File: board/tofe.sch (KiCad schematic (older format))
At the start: 16 parts, among them P301 TOFE I2C, P302 TOFE-8X, P303 DEBUG, U301 24AA01/24LC01B

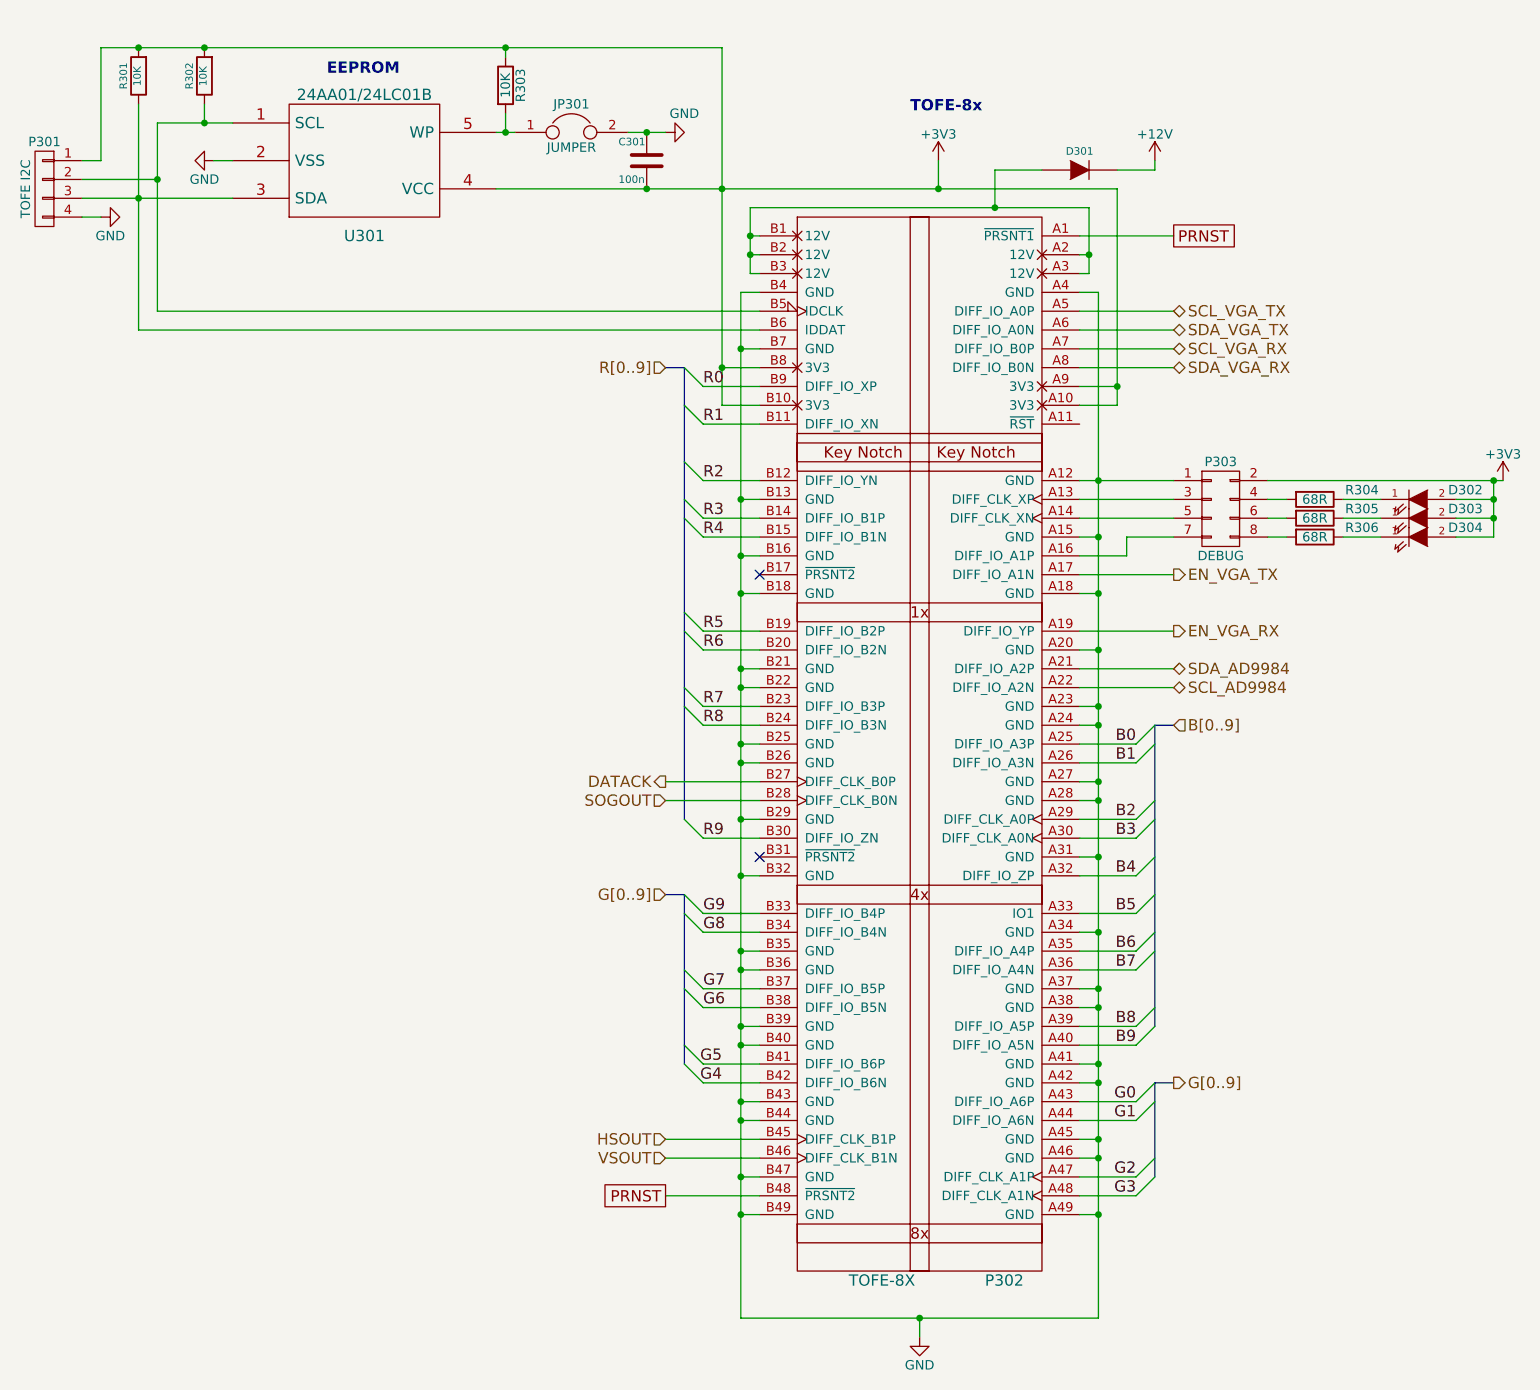
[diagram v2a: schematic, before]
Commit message: Lots of small tweaks.
 * Giving things better reference names.
 * Giving a bunch of nets names.
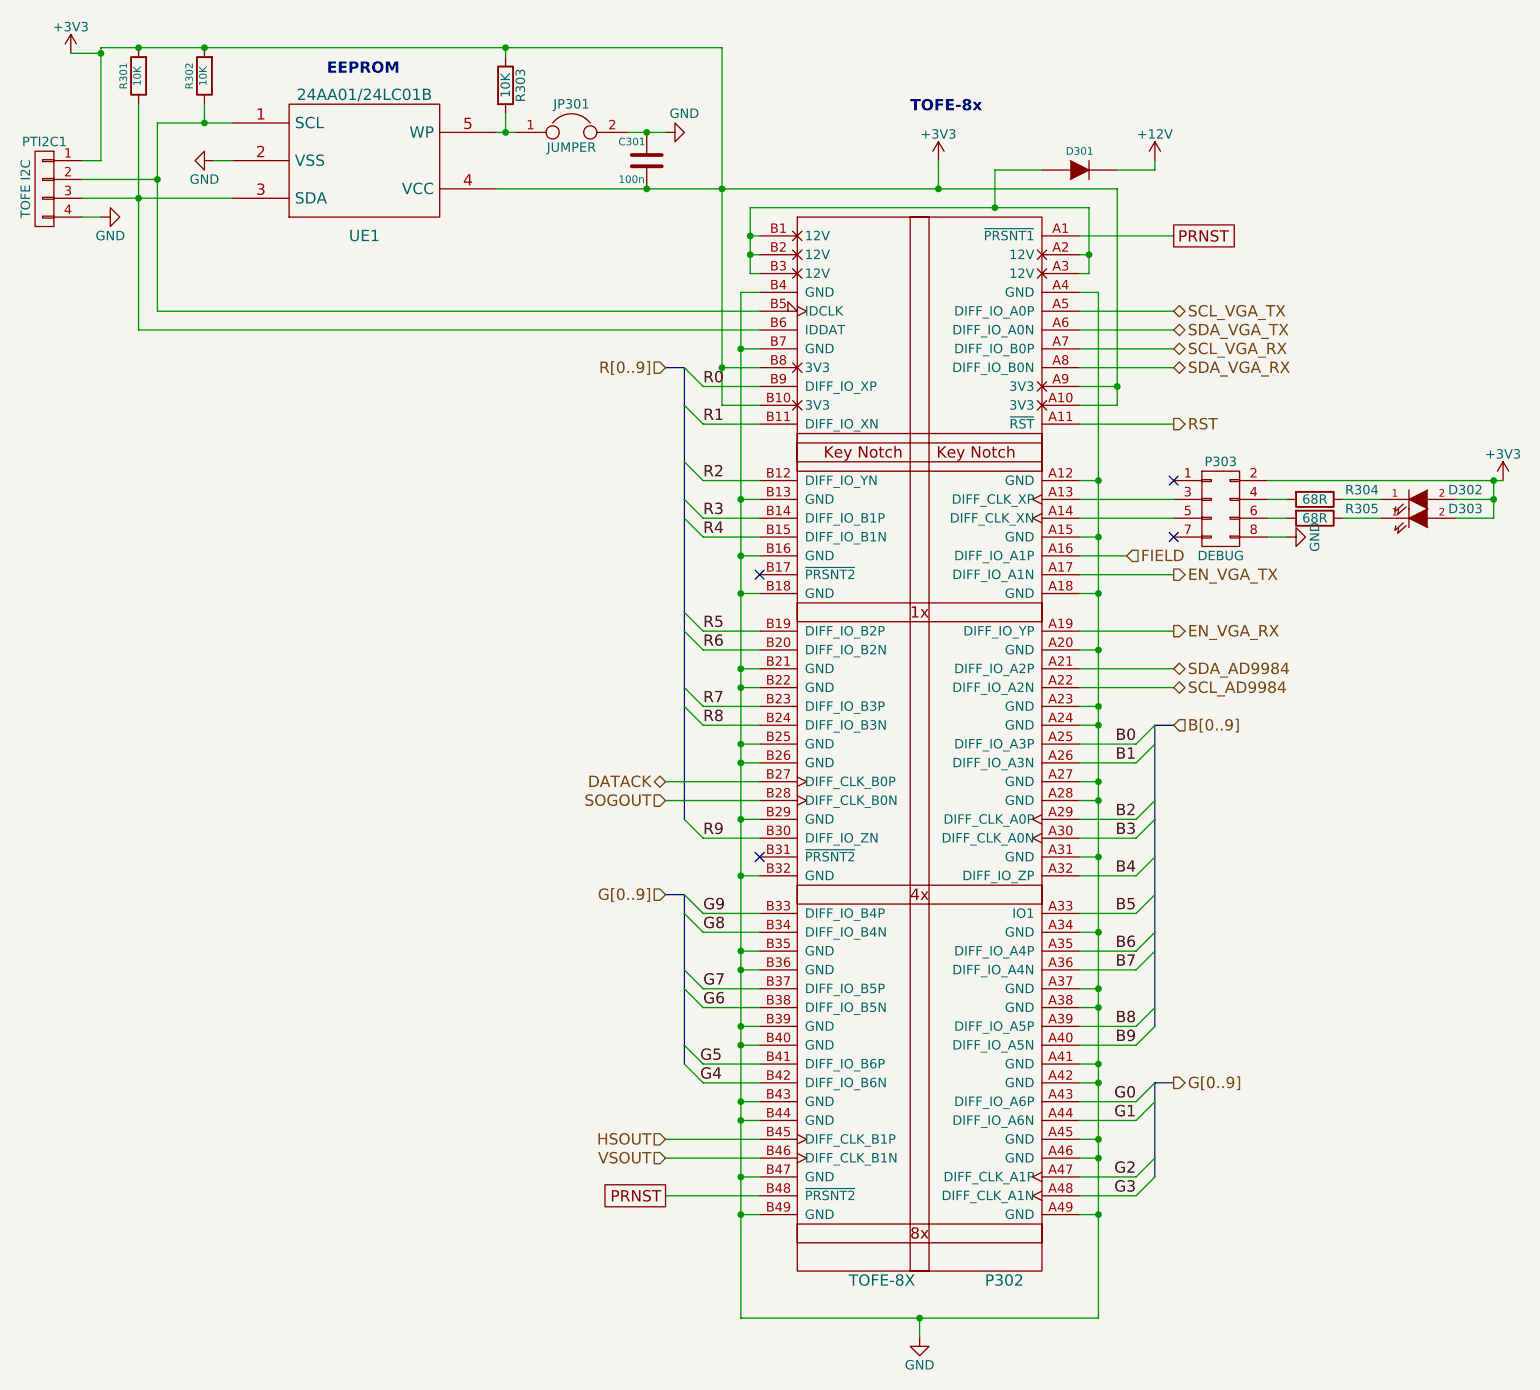
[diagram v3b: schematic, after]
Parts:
- removed D304: LED, LEDs:LED_0805, symbol LED
- removed R306: 68R, Resistors_SMD:R_0805_HandSoldering, symbol R
- renumbered P301 to PTI2C1, U301 to UE1
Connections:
- net GND: now also P303.8 (P8); no longer P303.1 (P1)
- net RST: now reaches P302.A11 (~RST)
- net at P303.7 (P7): no longer P302.A16 (DIFF_IO_A1P)
- new net FIELD: P302.A16 (DIFF_IO_A1P)
- no-connect marks 2 -> 4
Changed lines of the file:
@@
 $EndComp
 $Comp
-L 24AA01/24LC01B U301
+L 24AA01/24LC01B UE1
 U 1 1 561CAC90
 P 2500 1250
-F 0 "U301" H 2500 850 60  0000 C CNN
+F 0 "UE1" H 2500 850 60  0000 C CNN
 F 1 "24AA01/24LC01B" H 2500 1600 60  0000 C CNN
 F 2 "TO_SOT_Packages_SMD:SOT-23-5" H 2500 1250 60  0001 C CNN
@@
 Text HLabel 4100 4650 0    60   Input ~ 0
 SOGOUT
-Text HLabel 4100 4550 0    60   Output ~ 0
+Text HLabel 4100 4550 0    60   BiDi ~ 0
 DATACK
 Wire Wire Line
@@
 Connection ~ 6400 6850
 Connection ~ 5450 7400
-Wire Wire Line
-	6300 2950 6800 2950
 Connection ~ 6400 2950
 Wire Wire Line
@@
 Wire Wire Line
 	6300 3350 6550 3350
-Wire Wire Line
-	6550 3350 6550 3250
-Wire Wire Line
-	6550 3250 6800 3250
 $Comp
 L LED D302
@@
 Wire Wire Line
 	7700 3150 7900 3150
-$Comp
-L LED D304
-U 1 1 5692619B
-P 8100 3250
-F 0 "D304" H 8350 3300 50  0000 C CNN
-F 1 "LED" H 8100 3150 50  0001 C CNN
-F 2 "LEDs:LED_0805" H 8100 3250 50  0001 C CNN
-F 3 "" H 8100 3250 50  0000 C CNN
-	1    8100 3250
-	1    0    0    -1
-$EndComp
-$Comp
-L R R306
-U 1 1 569261A1
-P 7550 3250
-F 0 "R306" V 7500 3500 50  0000 C CNN
-F 1 "68R" V 7550 3250 50  0000 C CNN
-F 2 "Resistors_SMD:R_0805_HandSoldering" V 7480 3250 50  0001 C CNN
-F 3 "" H 7550 3250 50  0000 C CNN
-	1    7550 3250
-	0    1    1    0
-$EndComp
 Wire Wire Line
 	7300 3250 7400 3250
 Wire Wire Line
-	7700 3250 7900 3250
-Wire Wire Line
 	8300 3050 8500 3050
-Wire Wire Line
-	8500 3250 8500 2950
 Connection ~ 8500 2950
 Wire Wire Line
@@
 Connection ~ 8500 3050
 Wire Wire Line
-	8300 3250 8500 3250
-Connection ~ 8500 3150
-Wire Wire Line
 	7300 2950 8550 2950
 $Comp
-L CONN_01X04 P301
+L CONN_01X04 PTI2C1
 U 1 1 569310F0
 P 800 1400
-F 0 "P301" H 800 1650 50  0000 C CNN
+F 0 "PTI2C1" H 800 1650 50  0000 C CNN
 F 1 "TOFE I2C" V 900 1400 50  0000 C CNN
 F 2 "CON-SMD-2.54:HARWIN-M20-87-4x1" H 800 1400 50  0001 C CNN
@@
 	1    0    0    -1
 $EndComp
+Wire Wire Line
+	6300 2650 6800 2650
+Text HLabel 6800 2650 2    60   Output ~ 0
+RST
+Wire Wire Line
+	8500 3150 8500 2950
+Text HLabel 6550 3350 2    60   Input ~ 0
+FIELD
+$Comp
+L GND #PWR?
+U 1 1 579E0967
+P 7400 3250
+F 0 "#PWR?" H 7400 3000 50  0001 C CNN
+F 1 "GND" H 7400 3100 50  0000 C CNN
+F 2 "" H 7400 3250 50  0000 C CNN
+F 3 "" H 7400 3250 50  0000 C CNN
+	1    7400 3250
+	0    -1   -1   0
+$EndComp
+Wire Wire Line
+	6300 2950 6400 2950
+NoConn ~ 6800 2950
+NoConn ~ 6800 3250
+$Comp
+L +3V3 #PWR?
+U 1 1 579E0C0C
+P 940 680
+F 0 "#PWR?" H 940 530 50  0001 C CNN
+F 1 "+3V3" H 940 820 50  0000 C CNN
+F 2 "" H 940 680 60  0000 C CNN
+F 3 "" H 940 680 60  0000 C CNN
+	1    940  680
+	1    0    0    -1
+$EndComp
+Wire Wire Line
+	940  680  1100 680
+Connection ~ 1100 680
 $EndSCHEMATC
